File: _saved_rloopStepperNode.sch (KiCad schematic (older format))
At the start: 0 parts

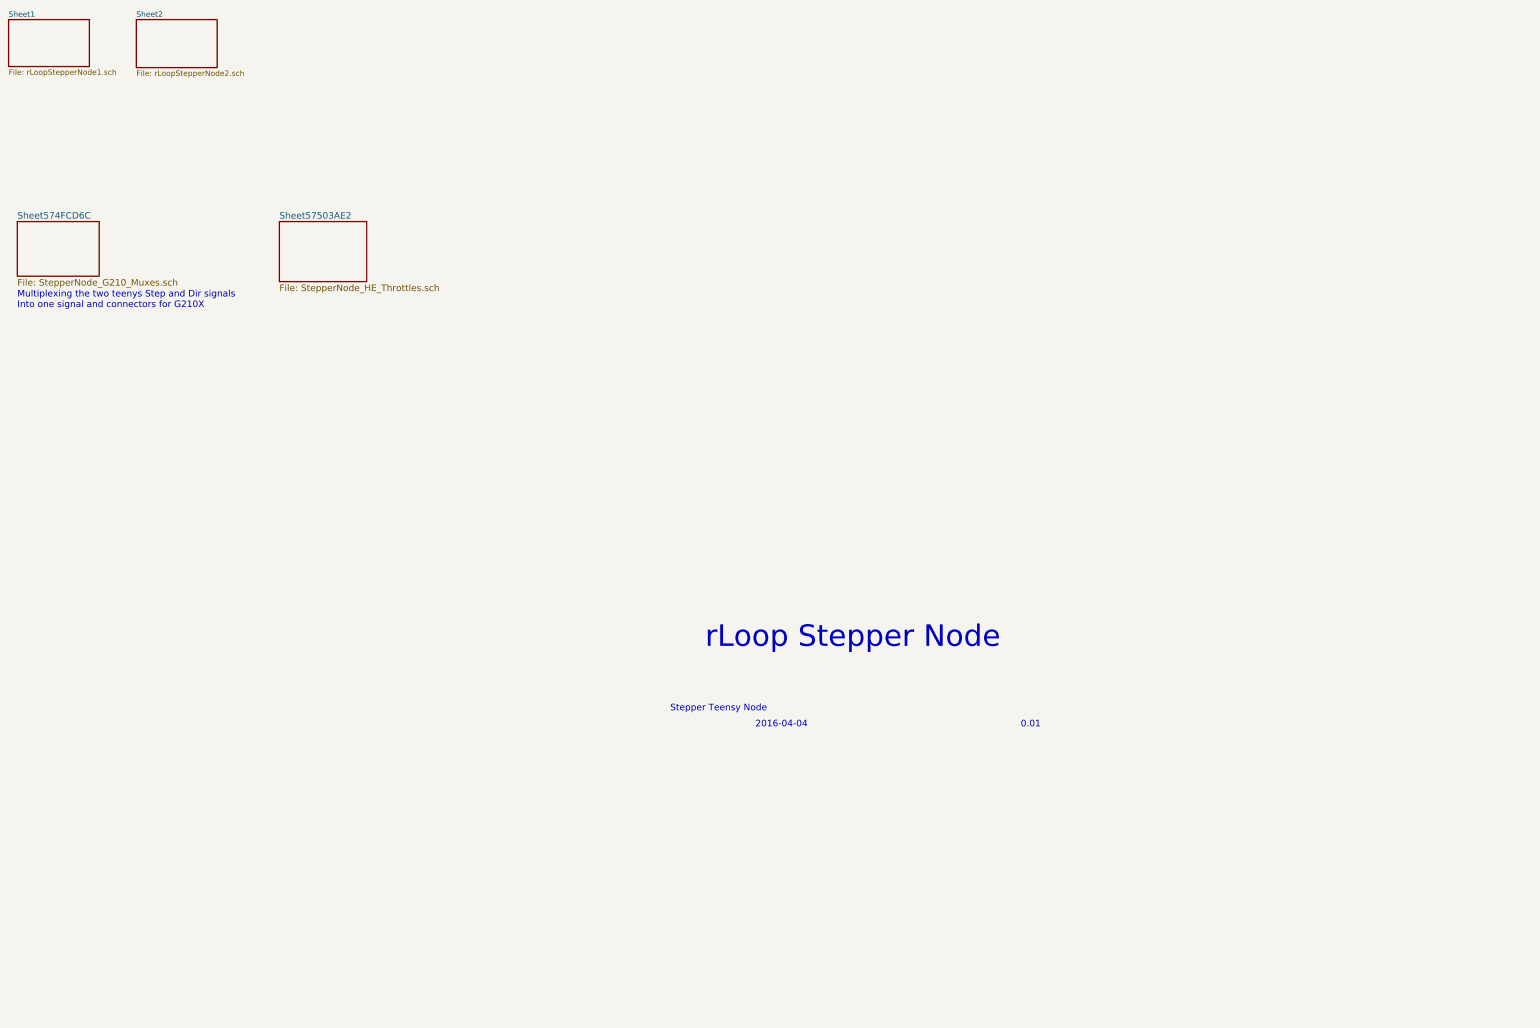
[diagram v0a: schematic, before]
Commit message: Add DAC Pages
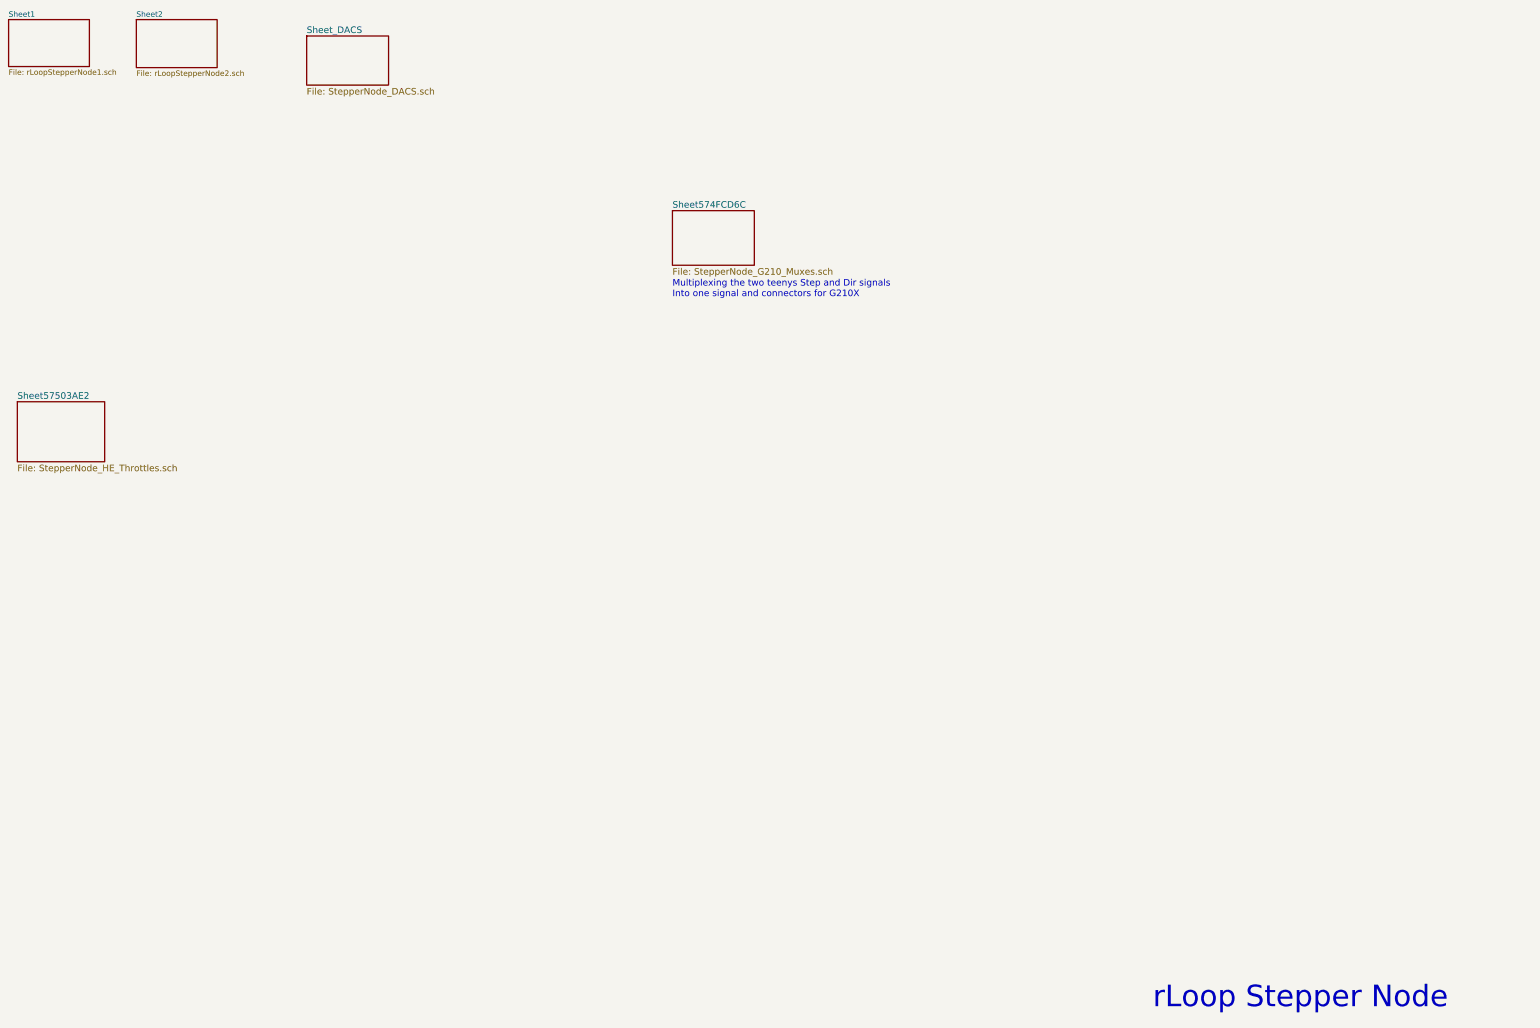
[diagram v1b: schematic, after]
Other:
- note removed: "0.01"
- note removed: "2016-04-04"
- note removed: "Stepper Teensy Node\n\n"
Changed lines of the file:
@@
 EELAYER 25 0
 EELAYER END
-$Descr A4 11693 8268
+$Descr A3 16535 11693
 encoding utf-8
-Sheet 1 5
-Title ""
+Sheet 1 6
+Title "Top Level"
 Date ""
-Rev ""
+Rev "1"
 Comp ""
 Comment1 ""
@@
 Comment4 ""
 $EndDescr
-Text Notes 7380 7590 0    60   ~ 0
-Stepper Teensy Node\n\n
-Text Notes 8160 7640 0    60   ~ 0
-2016-04-04
-Text Notes 10590 7640 0    60   ~ 0
-0.01
-Text Notes 7700 6920 0    197  ~ 0
+Text Notes 11800 10220 0    197  ~ 0
 rLoop Stepper Node\n
 $Sheet
@@
 $EndSheet
 $Sheet
-S 1400 3000 750  500
+S 7400 2900 750  500
 U 574FCD6D
 F0 "Sheet574FCD6C" 60
 F1 "StepperNode_G210_Muxes.sch" 60
 $EndSheet
-Text Notes 1400 3800 0    60   ~ 0
+Text Notes 7400 3700 0    60   ~ 0
 Multiplexing the two teenys Step and Dir signals\nInto one signal and connectors for G210X
 $Sheet
-S 3800 3000 800  550
+S 1400 4650 800  550
 U 57503AE3
 F0 "Sheet57503AE2" 60
 F1 "StepperNode_HE_Throttles.sch" 60
 $EndSheet
+$Sheet
+S 4050 1300 750  450
+U 5750595A
+F0 "Sheet_DACS" 60
+F1 "StepperNode_DACS.sch" 60
+$EndSheet
 $EndSCHEMATC
